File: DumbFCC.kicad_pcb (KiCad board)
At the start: 4 copper layers, 70 x 50 mm, 80 parts, among them J100 5V Input, J300 Distance Sensor, J402 SD port, J500 Debug, J501 UART, J502 I2C, J503 CAN port, J504 Motor, J505 Gimbal, J506 USB C, SW400 Mode Switch, SW401 Reset, U100 ADP3330ARTZ3.3-RL7, U200 STM32H573RIT6, U300 LIS2MDL, U301 LSM6DSL, U302 MS5607-02BA, U400 AT25DF321A-SH-T, U500 MCP2562T-E_SN, Y200 25MHz

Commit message: Update Outputs (release)
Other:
- board text added: "0.02mm"
- board text added: "0.035mm (1.00oz)"
- board text added: "0.07mm (2.00oz)"
- board text added: "0.1mm"
- board text added: "1.15mm"
- board text added: "B.Mask"
- board text added: "B.Paste"
- board text added: "B.Silkscreen"
- board text added: "Copper"
- board text added: "Core"
- board text added: "Dielectric"
- board text added: "Direct Printing"
- board text added: "F.Mask"
- board text added: "F.Paste"
- board text added: "F.Silkscreen"
- board text added: "FR4"
- board text added: "FR4_7628"
- board text added: "GBR"
- board text added: "Gerber"
- board text added: "L1 (Sig, PWR)"
- board text added: "L2 (GND)"
- board text added: "L3 (GND)"
- board text added: "L4 (Sig, PWR)"
- board text added: "Layer"
- board text added: "Legend"
- board text added: "Material"
- board text added: "Note: external layer thicknesses are specified after plating"
- board text added: "Paste Mask"
- board text added: "Plane"
- board text added: "Prepreg"
- board text added: "Signal"
- board text added: "Solder Mask"
- board text added: "Solder Resist"
- board text added: "Thickness"
- board text added: "Total thickness: 1.6mm"
- board text added: "Type"

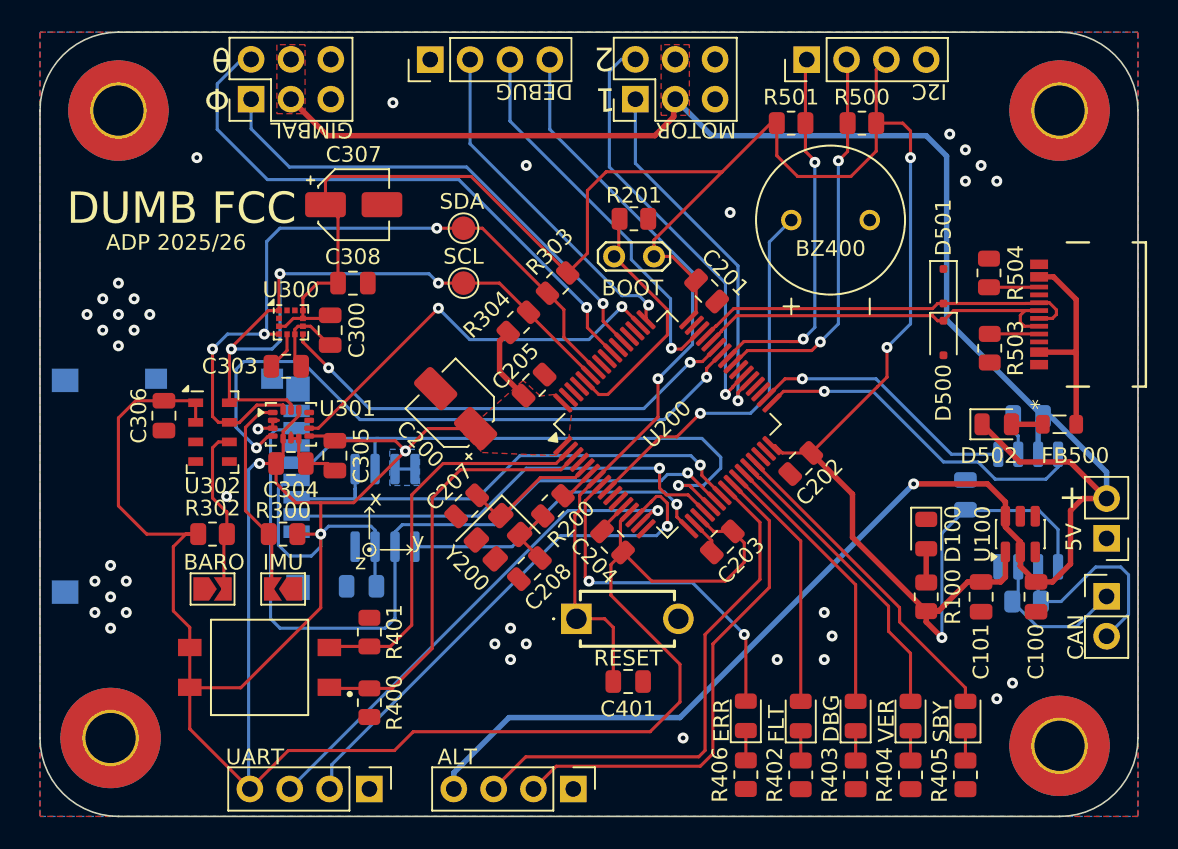
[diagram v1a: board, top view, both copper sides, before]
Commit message: [PCB][Fixed] Fixed wrong Diode footprint and Changed TVS diode package, also changed wrong footprint of CAN transiever chip. [Changed] Changed the FLASH chip to a different model due to a stocking issue
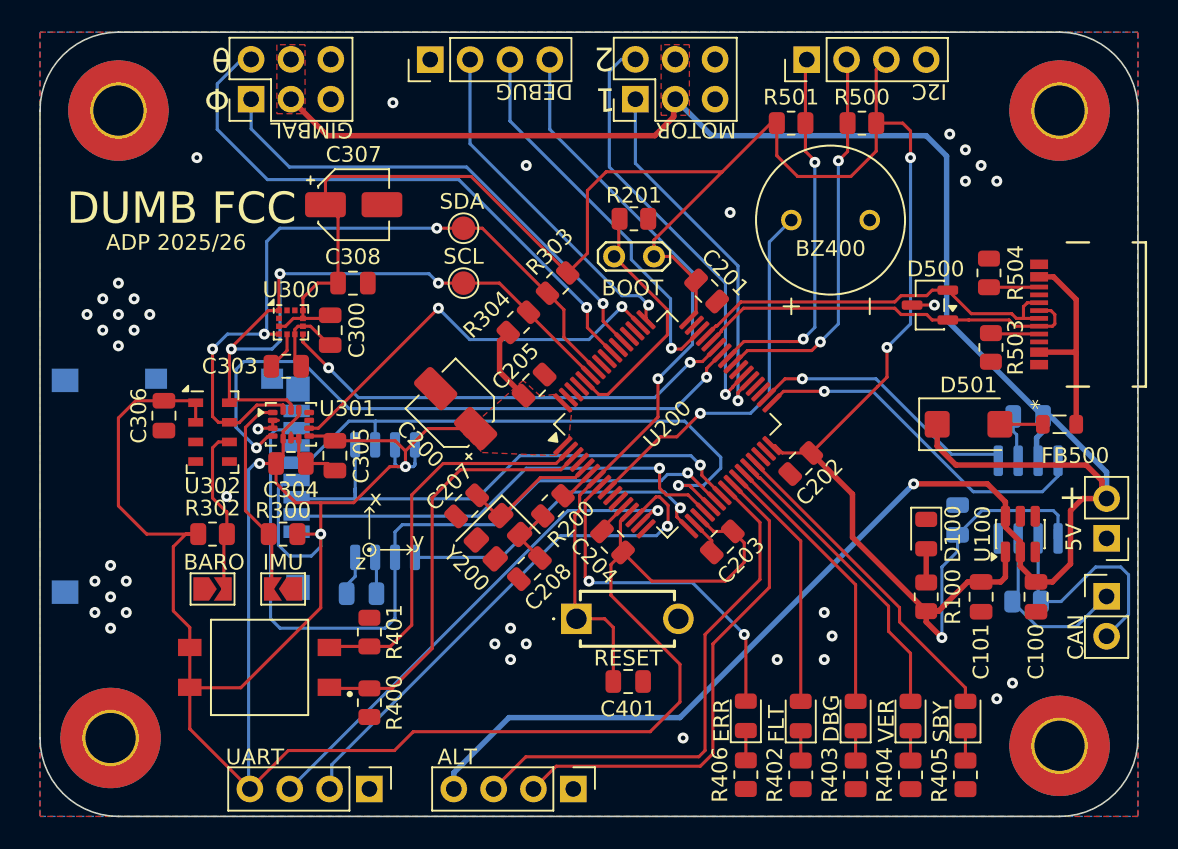
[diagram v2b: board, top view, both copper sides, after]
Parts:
- removed D502: D_Schottky, Diode_SMD:D_0805_2012Metric
- D500: value TVS -> ESDA6V1l-tp; footprint Diode_SMD:D_SOD-323F -> Package_TO_SOT_SMD:SOT-23-3
- D501: value TVS -> D_Schottky; footprint Diode_SMD:D_SOD-323F -> DO214AAC:P25_DO-214AC_SMA
- U400: value AT25DF321A-SH-T -> SST26VF064BT-104I/SM; footprint Package_SO:SOIC-8_3.9x4.9mm_P1.27mm -> Package_SO:SOIC-8_5.3x5.3mm_P1.27mm
- U500: footprint Package_SO:SOIC-8_5.3x5.3mm_P1.27mm -> Package_SO:SOIC-8_3.9x4.9mm_P1.27mm
- moved D501 8.94 mm to (174.2, 85.0), turned to 0 degrees
- moved D500 2.27 mm to (171.7, 77.4), turned to 180 degrees
- moved C501 1.68 mm to (173.5, 91.1)
- moved U500 0.70 mm to (178.0, 89.8)
- moved C400 0.47 mm to (135.5, 95.8)
- moved U400 0.43 mm to (137.0, 89.9)
- moved R503 0.09 mm to (175.6, 80.1)
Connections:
- D500 pad 2: GND -> /Project Architecture/Connections/USB_D+
- D501 pad 1: GND -> +5V
- D501 pad 2: /Project Architecture/Connections/USB_D+ -> Net-(D501-A)
- FB500 pad 2: Net-(D502-A) -> Net-(D501-A)
- J500 pad 2: /Project Architecture/Connections/SWDIO -> /Project Architecture/Connections/SWCLK
- J500 pad 3: /Project Architecture/Connections/SWCLK -> /Project Architecture/Connections/SWDIO
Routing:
- net +5V: track 143.9 -> 148.6 mm
- net GND: track 18.9 -> 23.2 mm, vias 38 -> 39
- net +3V3: track 335.6 -> 332.5 mm
- net Net-(D501-A): track 0.00 -> 2.74 mm
- net Net-(D502-A): track 2.00 -> 0.00 mm
- net /Project Architecture/Connections/CANL: track 13.8 -> 15.6 mm
- net /Project Architecture/Connections/CANH: track 9.84 -> 11.7 mm
- net /Project Architecture/MCU/SPI_MOSI: track 32.5 -> 34.2 mm
- net /Project Architecture/Connections/USB_D-: track 24.2 -> 25.1 mm
- net /Project Architecture/Connections/CAN_RX: track 22.0 -> 22.6 mm
- net /Project Architecture/MCU/MAG_INT: track 30.2 -> 29.7 mm
- net /Project Architecture/MCU/IMU_INT_1: track 41.7 -> 41.2 mm
- removed copper zone on B.Cu, net +3V3

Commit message: [pcb][changed] updated footprints that were incorrect, changed flash memory module due to stock issues
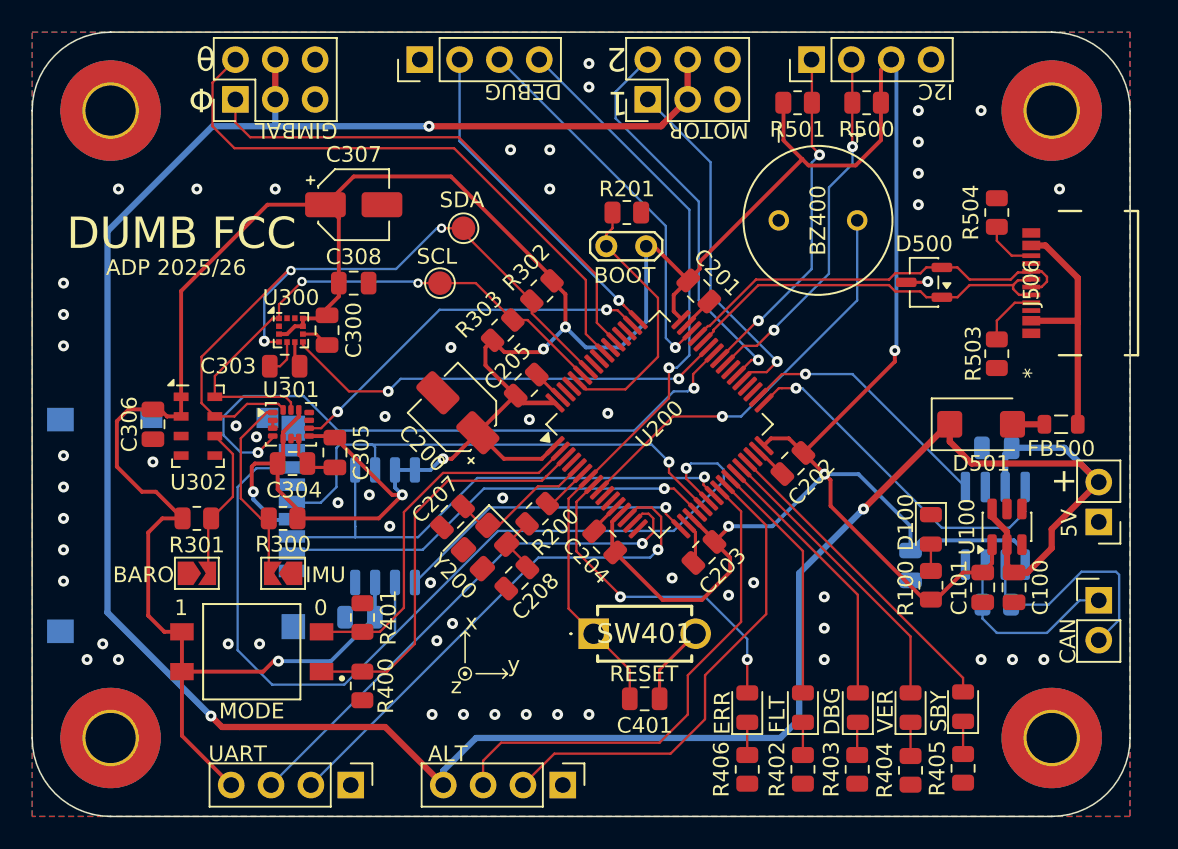
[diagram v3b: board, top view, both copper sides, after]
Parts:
- removed R304: 10k, Resistor_SMD:R_0805_2012Metric
- added R301: 10k, Resistor_SMD:R_0805_2012Metric, F.Cu at (125.0, 91.0)
- moved H203 60.5 mm to (119.5, 105.0)
- moved H202 60.0 mm to (179.5, 105.0)
- moved R302 26.1 mm to (147.0, 76.5), turned to -135 degrees
- moved R303 4.61 mm to (144.5, 79.0), turned to 45 degrees
- moved C501 4.17 mm to (170.5, 94.0), turned to 90 degrees
- moved R504 3.88 mm to (176.0, 71.5)
- moved C500 2.83 mm to (176.0, 86.5)
- moved U500 2.68 mm to (175.9, 91.5)
- moved J402 2.52 mm to (123.7, 91.5)
- moved J506 2.06 mm to (181.5, 76.0)
- moved R502 1.91 mm to (176.0, 96.5)
- moved U400 1.60 mm to (137.0, 91.5)
- moved C100 1.52 mm to (177.1, 95.4)
- moved C401 1.52 mm to (153.6, 102.5)
- moved C400 1.50 mm to (135.4, 97.3), turned to 180 degrees
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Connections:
- net Net-(FB500-Pad1) renamed /Project Architecture/Connections/V_BUS
- C400 pad 1: GND -> +3V3
- C400 pad 2: +3V3 -> GND
- R302 pad 2: Net-(JP302-B) -> /Project Architecture/MCU/I2C_SENS_SDA
- R303 pad 2: /Project Architecture/MCU/I2C_SENS_SDA -> /Project Architecture/MCU/I2C_SENS_SCL
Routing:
- net +3V3: track 332.5 -> 299.5 mm, vias 6 -> 9
- net +5V: track 148.6 -> 179.3 mm, vias 1 -> 3
- net /Project Architecture/MCU/SPI_MISO: track 50.0 -> 60.9 mm
- net /Project Architecture/MCU/I2C_SENS_SCL: track 44.7 -> 35.8 mm, vias 3 -> 2
- net /Project Architecture/MCU/SPI_SCK: track 37.5 -> 33.4 mm
- net GND: track 23.2 -> 26.4 mm, vias 39 -> 57
- net /Project Architecture/Connections/V_BUS: track 13.3 -> 16.2 mm
- net /Project Architecture/MCU/IMU_INT_2: track 26.5 -> 24.2 mm
- net /Project Architecture/MCU/BUZZ: track 24.6 -> 26.5 mm
- net /Project Architecture/Connections/PWM_2: track 27.4 -> 25.6 mm
- net /Project Architecture/Connections/I2C_PERIPH_SCL: track 23.8 -> 22.0 mm
- net /Project Architecture/MCU/SW_MODE_2: track 25.3 -> 23.6 mm
- net /Project Architecture/Connections/I2C_PERIPH_SDA: track 24.9 -> 23.4 mm
- net /Project Architecture/Connections/NRST: track 48.4 -> 49.8 mm
- net /Project Architecture/Connections/GIMB_PITCH: track 31.9 -> 33.3 mm, vias 1 -> 0
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- removed copper zone on F.Cu, net +3V3
- removed copper zone on F.Cu, net +5V
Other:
- board text added: "0"
- board text added: "MODE"
